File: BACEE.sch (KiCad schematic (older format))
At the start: 13 parts

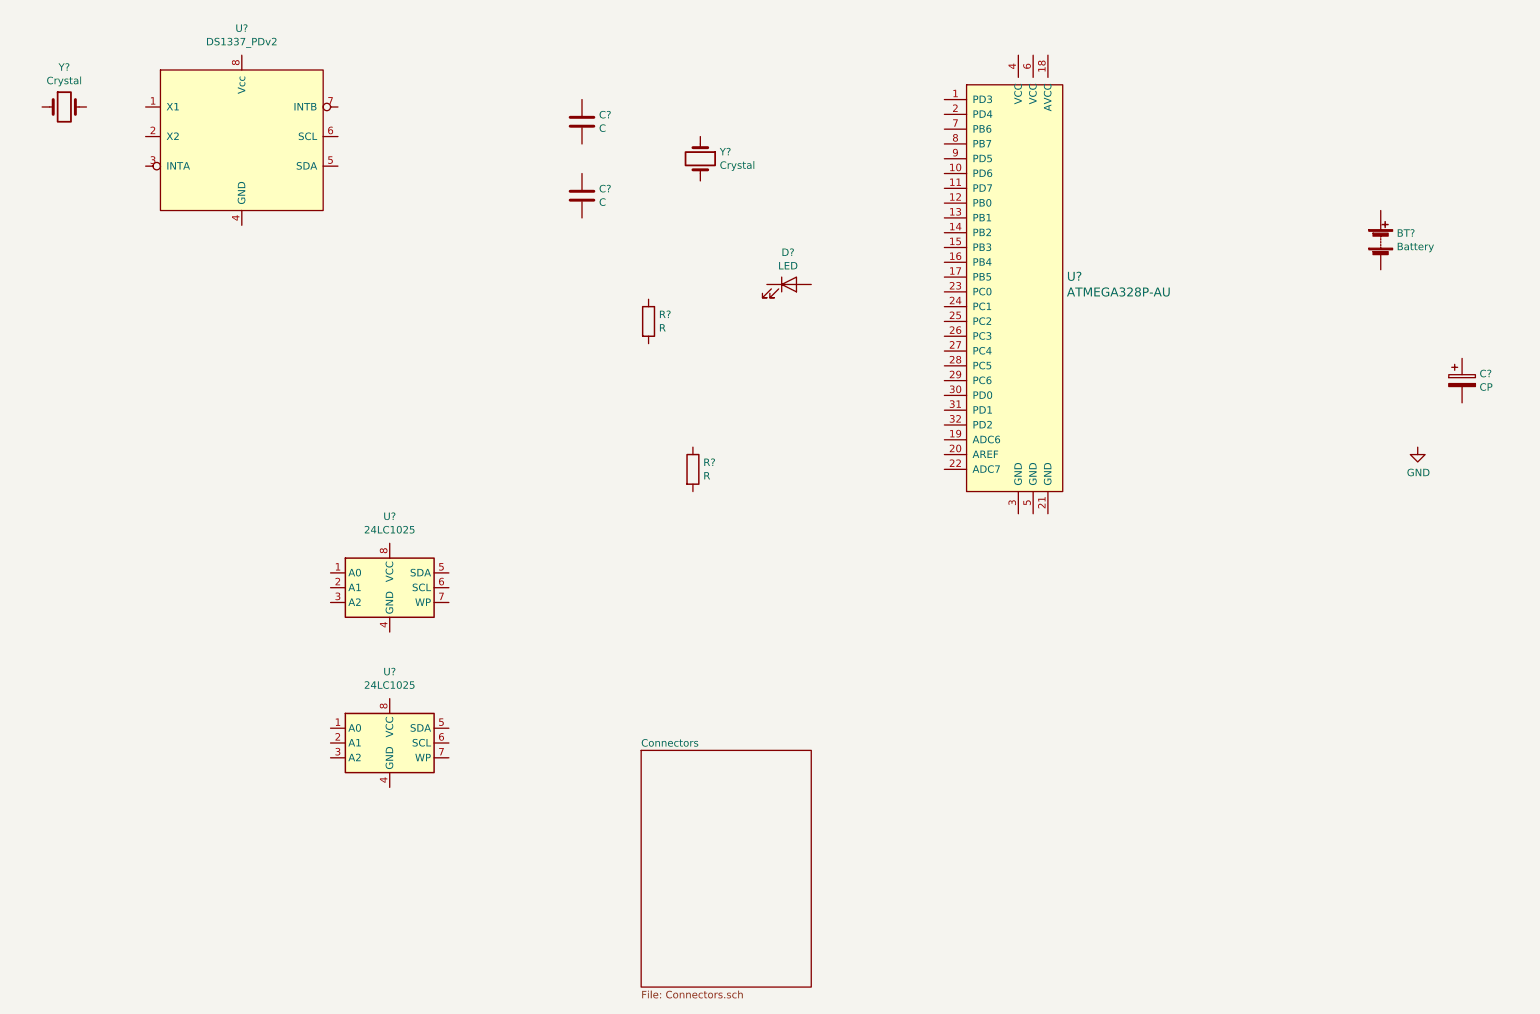
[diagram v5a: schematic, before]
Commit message: Addded footprints
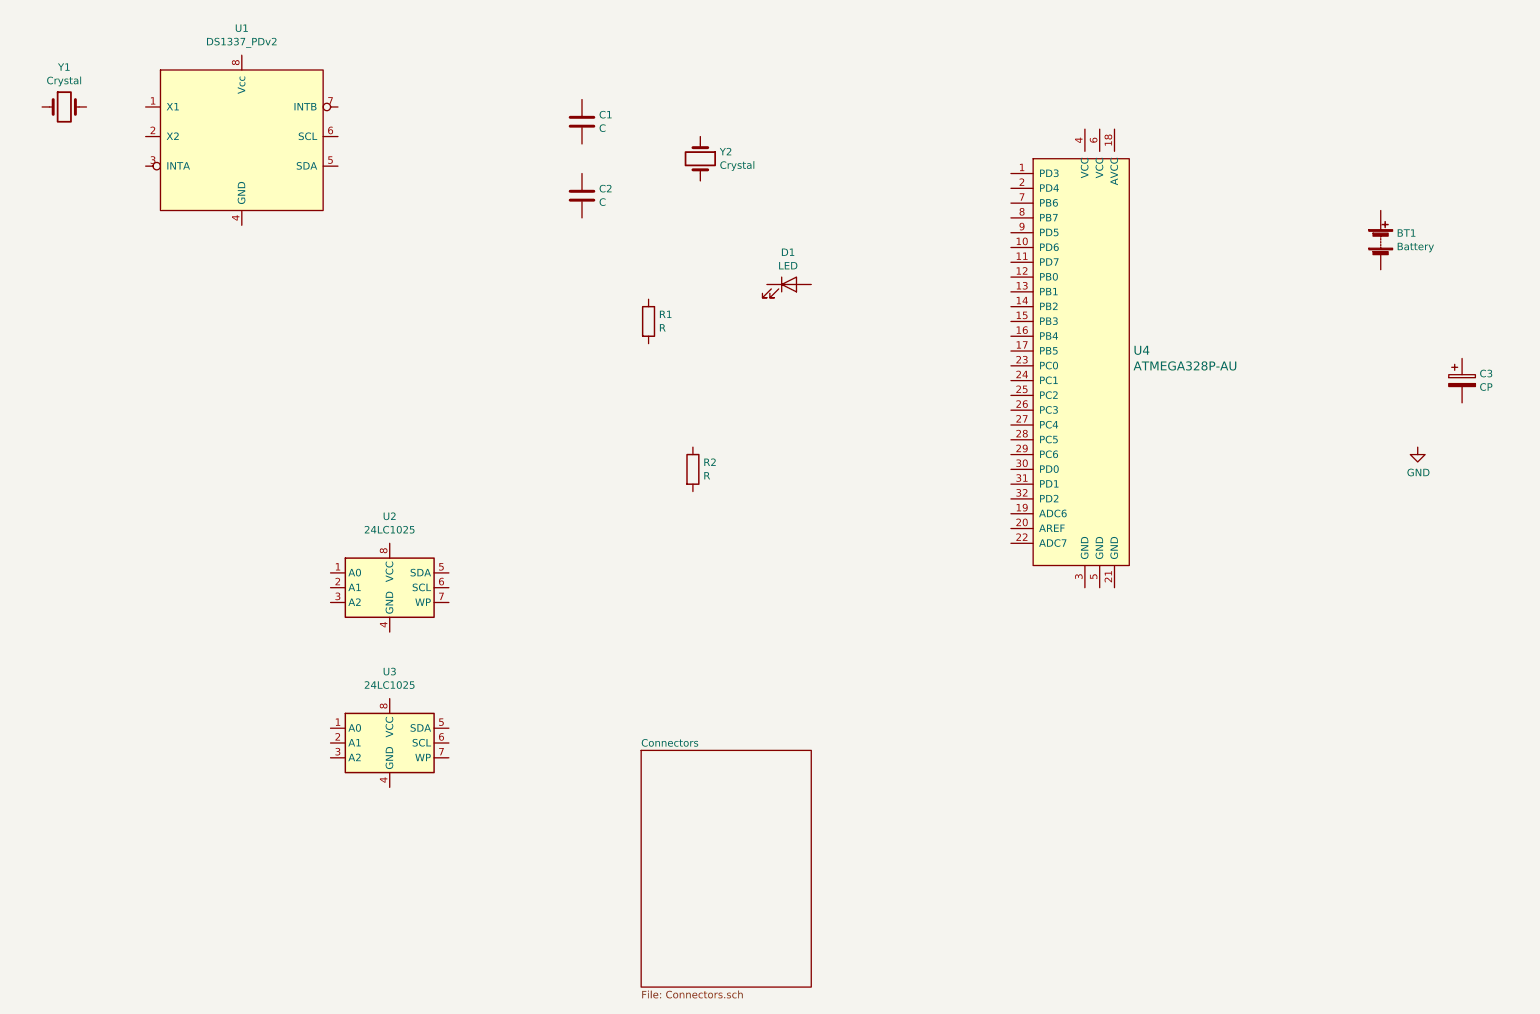
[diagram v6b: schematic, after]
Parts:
- removed U?: ATMEGA328P-AU, digikey-footprints:TQFP-32_7x7mm, symbol dk_Embedded-Microcontrollers:ATMEGA328P-AU
- added U4: ATMEGA328P-AU, digikey-footprints:TQFP-32_7x7mm, symbol dk_Embedded-Microcontrollers:ATMEGA328P-AU
- BT1: renamed from BT?; footprint (none) -> Connector_PinHeader_2.54mm:PinHeader_1x02_P2.54mm_Vertical
- C1, C2, C3: renamed from C?; footprint (none) -> Capacitor_SMD:C_0805_2012Metric_Pad1.15x1.40mm_HandSolder
- D1: renamed from D?; footprint (none) -> LED_SMD:LED_0805_2012Metric_Pad1.15x1.40mm_HandSolder
- R1, R2: renamed from R?; footprint (none) -> Resistor_SMD:R_0805_2012Metric_Pad1.15x1.40mm_HandSolder
- U1, U2: renamed from U?; footprint (none) -> Package_SO:SOIJ-8_5.3x5.3mm_P1.27mm
- U3: renamed from U?; footprint (none) -> Package_SO:SO-8_5.3x6.2mm_P1.27mm
- Y1: renamed from Y?; footprint (none) -> Crystal:Crystal_SMD_MicroCrystal_CC7V-T1A-2Pin_3.2x1.5mm
- Y2: renamed from Y?; footprint (none) -> Crystal:Crystal_SMD_5032-2Pin_5.0x3.2mm_HandSoldering
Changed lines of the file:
@@
 $EndDescr
 $Comp
-L Device:Battery BT?
+L Device:Battery BT1
 U 1 1 5EC0DCA7
 P 9800 2600
-F 0 "BT?" H 9908 2646 50  0000 L CNN
+F 0 "BT1" H 9908 2646 50  0000 L CNN
 F 1 "Battery" H 9908 2555 50  0000 L CNN
-F 2 "" V 9800 2660 50  0001 C CNN
+F 2 "Connector_PinHeader_2.54mm:PinHeader_1x02_P2.54mm_Vertical" V 9800 2660 50  0001 C CNN
 F 3 "~" V 9800 2660 50  0001 C CNN
 	1    9800 2600
@@
 $EndComp
 $Comp
-L Device:C C?
+L Device:C C1
 U 1 1 5EC0FEED
 P 4400 1800
-F 0 "C?" H 4515 1846 50  0000 L CNN
+F 0 "C1" H 4515 1846 50  0000 L CNN
 F 1 "C" H 4515 1755 50  0000 L CNN
-F 2 "" H 4438 1650 50  0001 C CNN
+F 2 "Capacitor_SMD:C_0805_2012Metric_Pad1.15x1.40mm_HandSolder" H 4438 1650 50  0001 C CNN
 F 3 "~" H 4400 1800 50  0001 C CNN
 	1    4400 1800
@@
 $EndComp
 $Comp
-L Device:C C?
+L Device:C C2
 U 1 1 5EC1064E
 P 4400 2300
-F 0 "C?" H 4515 2346 50  0000 L CNN
+F 0 "C2" H 4515 2346 50  0000 L CNN
 F 1 "C" H 4515 2255 50  0000 L CNN
-F 2 "" H 4438 2150 50  0001 C CNN
+F 2 "Capacitor_SMD:C_0805_2012Metric_Pad1.15x1.40mm_HandSolder" H 4438 2150 50  0001 C CNN
 F 3 "~" H 4400 2300 50  0001 C CNN
 	1    4400 2300
@@
 $EndComp
 $Comp
-L Device:CP C?
+L Device:CP C3
 U 1 1 5EC10D42
 P 10350 3550
-F 0 "C?" H 10468 3596 50  0000 L CNN
+F 0 "C3" H 10468 3596 50  0000 L CNN
 F 1 "CP" H 10468 3505 50  0000 L CNN
-F 2 "" H 10388 3400 50  0001 C CNN
+F 2 "Capacitor_SMD:C_0805_2012Metric_Pad1.15x1.40mm_HandSolder" H 10388 3400 50  0001 C CNN
 F 3 "~" H 10350 3550 50  0001 C CNN
 	1    10350 3550
@@
 $EndComp
 $Comp
-L Device:LED D?
+L Device:LED D1
 U 1 1 5EC11BF2
 P 5800 2900
-F 0 "D?" H 5793 3116 50  0000 C CNN
+F 0 "D1" H 5793 3116 50  0000 C CNN
 F 1 "LED" H 5793 3025 50  0000 C CNN
-F 2 "" H 5800 2900 50  0001 C CNN
+F 2 "LED_SMD:LED_0805_2012Metric_Pad1.15x1.40mm_HandSolder" H 5800 2900 50  0001 C CNN
 F 3 "~" H 5800 2900 50  0001 C CNN
 	1    5800 2900
@@
 $EndComp
 $Comp
-L Device:R R?
+L Device:R R1
 U 1 1 5EC1258B
 P 4850 3150
-F 0 "R?" H 4920 3196 50  0000 L CNN
+F 0 "R1" H 4920 3196 50  0000 L CNN
 F 1 "R" H 4920 3105 50  0000 L CNN
-F 2 "" V 4780 3150 50  0001 C CNN
+F 2 "Resistor_SMD:R_0805_2012Metric_Pad1.15x1.40mm_HandSolder" V 4780 3150 50  0001 C CNN
 F 3 "~" H 4850 3150 50  0001 C CNN
 	1    4850 3150
@@
 $EndComp
 $Comp
-L Device:R R?
+L Device:R R2
 U 1 1 5EC1288A
 P 5150 4150
-F 0 "R?" H 5220 4196 50  0000 L CNN
+F 0 "R2" H 5220 4196 50  0000 L CNN
 F 1 "R" H 5220 4105 50  0000 L CNN
-F 2 "" V 5080 4150 50  0001 C CNN
+F 2 "Resistor_SMD:R_0805_2012Metric_Pad1.15x1.40mm_HandSolder" V 5080 4150 50  0001 C CNN
 F 3 "~" H 5150 4150 50  0001 C CNN
 	1    5150 4150
@@
 $EndComp
 $Comp
-L Memory_EEPROM:24LC1025 U?
+L Memory_EEPROM:24LC1025 U2
 U 1 1 5EC12FEA
 P 3100 4950
-F 0 "U?" H 3100 5431 50  0000 C CNN
+F 0 "U2" H 3100 5431 50  0000 C CNN
 F 1 "24LC1025" H 3100 5340 50  0000 C CNN
-F 2 "" H 3100 4950 50  0001 C CNN
+F 2 "Package_SO:SOIJ-8_5.3x5.3mm_P1.27mm" H 3100 4950 50  0001 C CNN
 F 3 "http://ww1.microchip.com/downloads/en/DeviceDoc/21941B.pdf" H 3100 4950 50  0001 C CNN
 	1    3100 4950
@@
 $EndSheet
 $Comp
-L dk_Embedded-Microcontrollers:ATMEGA328P-AU U?
-U 1 1 5EC1AF7B
-P 7350 2950
-F 0 "U?" H 7678 3053 60  0000 L CNN
-F 1 "ATMEGA328P-AU" H 7678 2947 60  0000 L CNN
-F 2 "digikey-footprints:TQFP-32_7x7mm" H 7550 3150 60  0001 L CNN
-F 3 "http://www.microchip.com/mymicrochip/filehandler.aspx?ddocname=en608326" H 7550 3250 60  0001 L CNN
-F 4 "ATMEGA328P-AU-ND" H 7550 3350 60  0001 L CNN "Digi-Key_PN"
-F 5 "ATMEGA328P-AU" H 7550 3450 60  0001 L CNN "MPN"
-F 6 "Integrated Circuits (ICs)" H 7550 3550 60  0001 L CNN "Category"
-F 7 "Embedded - Microcontrollers" H 7550 3650 60  0001 L CNN "Family"
-F 8 "http://www.microchip.com/mymicrochip/filehandler.aspx?ddocname=en608326" H 7550 3750 60  0001 L CNN "DK_Datasheet_Link"
-F 9 "/product-detail/en/microchip-technology/ATMEGA328P-AU/ATMEGA328P-AU-ND/1832260" H 7550 3850 60  0001 L CNN "DK_Detail_Page"
-F 10 "IC MCU 8BIT 32KB FLASH 32TQFP" H 7550 3950 60  0001 L CNN "Description"
-F 11 "Microchip Technology" H 7550 4050 60  0001 L CNN "Manufacturer"
-F 12 "Active" H 7550 4150 60  0001 L CNN "Status"
-	1    7350 2950
-	1    0    0    -1
-$EndComp
-$Comp
-L Arduino-Library:DS1337_PDv2 U?
+L Arduino-Library:DS1337_PDv2 U1
 U 1 1 5EC1F02F
 P 2100 1900
-F 0 "U?" H 2100 2631 50  0000 C CNN
+F 0 "U1" H 2100 2631 50  0000 C CNN
 F 1 "DS1337_PDv2" H 2100 2540 50  0000 C CNN
-F 2 "" H 3050 2400 50  0001 C CNN
+F 2 "Package_SO:SOIJ-8_5.3x5.3mm_P1.27mm" H 3050 2400 50  0001 C CNN
 F 3 "https://4donline.ihs.com/images/VipMasterIC/IC/MAXM/MAXM-S-A0000633411/MAXM-S-A0000771822-1.pdf?hkey=52A5661711E402568146F3353EA87419" H 3050 2400 50  0001 C CNN
 	1    2100 1900
@@
 $EndComp
 $Comp
-L Device:Crystal Y?
+L Device:Crystal Y1
 U 1 1 5EC1F9D8
 P 900 1700
-F 0 "Y?" H 900 1968 50  0000 C CNN
+F 0 "Y1" H 900 1968 50  0000 C CNN
 F 1 "Crystal" H 900 1877 50  0000 C CNN
-F 2 "" H 900 1700 50  0001 C CNN
+F 2 "Crystal:Crystal_SMD_MicroCrystal_CC7V-T1A-2Pin_3.2x1.5mm" H 900 1700 50  0001 C CNN
 F 3 "~" H 900 1700 50  0001 C CNN
 	1    900  1700
@@
 $EndComp
 $Comp
-L Device:Crystal Y?
+L Device:Crystal Y2
 U 1 1 5EC2101F
 P 5200 2050
-F 0 "Y?" V 5154 2181 50  0000 L CNN
+F 0 "Y2" V 5154 2181 50  0000 L CNN
 F 1 "Crystal" V 5245 2181 50  0000 L CNN
-F 2 "" H 5200 2050 50  0001 C CNN
+F 2 "Crystal:Crystal_SMD_5032-2Pin_5.0x3.2mm_HandSoldering" H 5200 2050 50  0001 C CNN
 F 3 "~" H 5200 2050 50  0001 C CNN
 	1    5200 2050
@@
 $EndComp
 $Comp
-L Memory_EEPROM:24LC1025 U?
+L Memory_EEPROM:24LC1025 U3
 U 1 1 5EC29420
 P 3100 6000
-F 0 "U?" H 3100 6481 50  0000 C CNN
+F 0 "U3" H 3100 6481 50  0000 C CNN
 F 1 "24LC1025" H 3100 6390 50  0000 C CNN
-F 2 "" H 3100 6000 50  0001 C CNN
+F 2 "Package_SO:SO-8_5.3x6.2mm_P1.27mm" H 3100 6000 50  0001 C CNN
 F 3 "http://ww1.microchip.com/downloads/en/DeviceDoc/21941B.pdf" H 3100 6000 50  0001 C CNN
 	1    3100 6000
@@
 $EndComp
 $Comp
-L power:GND #PWR?
+L power:GND #PWR0101
 U 1 1 5EC3997C
 P 10050 4000
-F 0 "#PWR?" H 10050 3750 50  0001 C CNN
+F 0 "#PWR0101" H 10050 3750 50  0001 C CNN
 F 1 "GND" H 10055 3827 50  0000 C CNN
 F 2 "" H 10050 4000 50  0001 C CNN
@@
 	1    0    0    -1
 $EndComp
+$Comp
+L dk_Embedded-Microcontrollers:ATMEGA328P-AU U4
+U 1 1 5EC48D6C
+P 7800 3450
+F 0 "U4" H 8128 3553 60  0000 L CNN
+F 1 "ATMEGA328P-AU" H 8128 3447 60  0000 L CNN
+F 2 "digikey-footprints:TQFP-32_7x7mm" H 8000 3650 60  0001 L CNN
+F 3 "http://www.microchip.com/mymicrochip/filehandler.aspx?ddocname=en608326" H 8000 3750 60  0001 L CNN
+F 4 "ATMEGA328P-AU-ND" H 8000 3850 60  0001 L CNN "Digi-Key_PN"
+F 5 "ATMEGA328P-AU" H 8000 3950 60  0001 L CNN "MPN"
+F 6 "Integrated Circuits (ICs)" H 8000 4050 60  0001 L CNN "Category"
+F 7 "Embedded - Microcontrollers" H 8000 4150 60  0001 L CNN "Family"
+F 8 "http://www.microchip.com/mymicrochip/filehandler.aspx?ddocname=en608326" H 8000 4250 60  0001 L CNN "DK_Datasheet_Link"
+F 9 "/product-detail/en/microchip-technology/ATMEGA328P-AU/ATMEGA328P-AU-ND/1832260" H 8000 4350 60  0001 L CNN "DK_Detail_Page"
+F 10 "IC MCU 8BIT 32KB FLASH 32TQFP" H 8000 4450 60  0001 L CNN "Description"
+F 11 "Microchip Technology" H 8000 4550 60  0001 L CNN "Manufacturer"
+F 12 "Active" H 8000 4650 60  0001 L CNN "Status"
+	1    7800 3450
+	1    0    0    -1
+$EndComp
